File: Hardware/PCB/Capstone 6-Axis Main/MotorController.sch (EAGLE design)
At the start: 56 parts, among them CON3 TI-JTAG-CTI-20, J1 768250004CON_768250004_MOL, J2 768250004CON_768250004_MOL, J3 MF-CON-2.54mm-01x03, J4 MF-CON-2.54mm-01x03, J5 MF-CON-2.54mm-01x03, J6 MF-CON-2.54mm-01x03, J7 MF-CON-2.54mm-01x03, J8 MF-CON-2.54mm-01x04, Q2 20MHz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

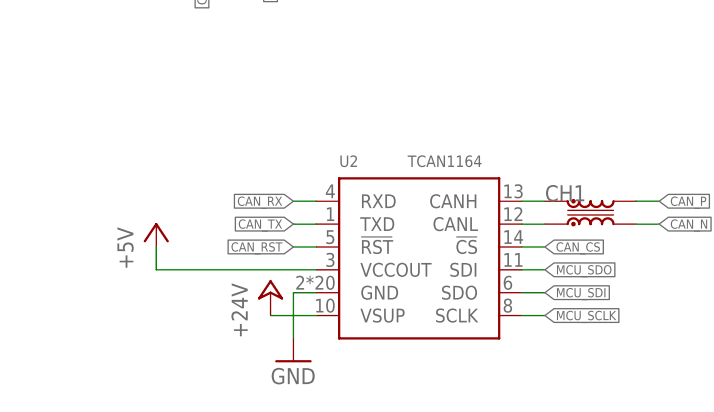
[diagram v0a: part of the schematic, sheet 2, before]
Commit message: Updated PCBs and added custom libraries
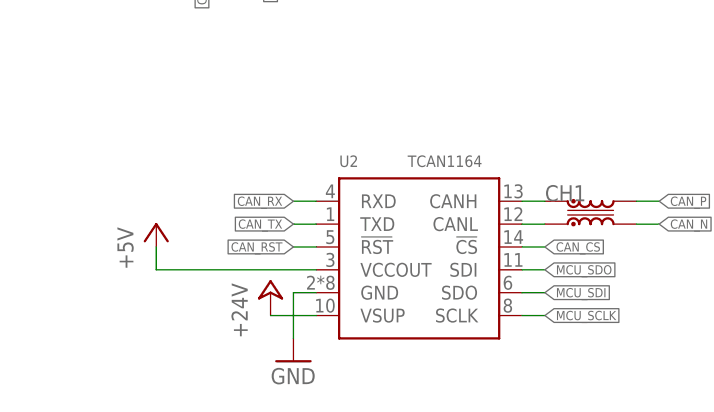
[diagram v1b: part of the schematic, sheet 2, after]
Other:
- moved on the sheet: U2
